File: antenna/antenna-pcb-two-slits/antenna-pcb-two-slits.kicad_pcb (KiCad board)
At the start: 2 copper layers, 97 x 97 mm, 11 parts, among them J1 SMA Connector Male, U1 HHM1589D1

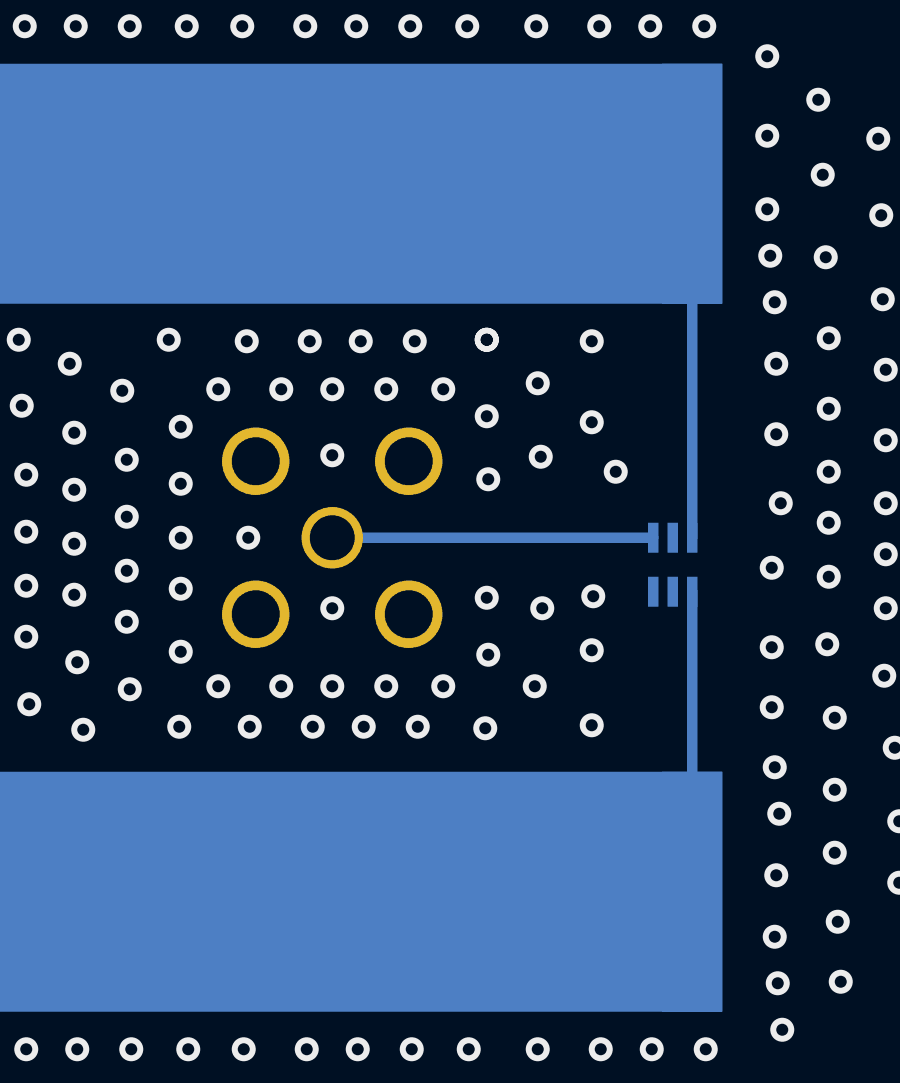
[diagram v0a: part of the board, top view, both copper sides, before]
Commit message: modify antenna pcbs and drc checked
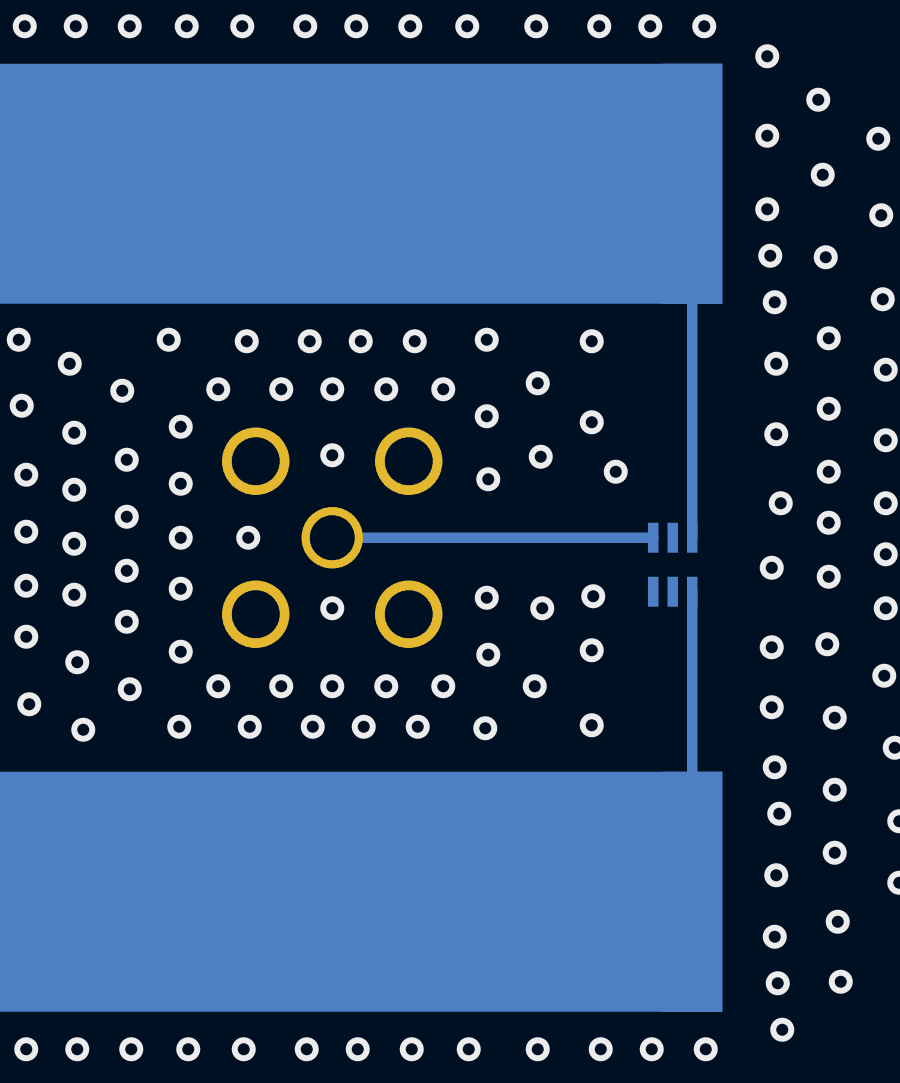
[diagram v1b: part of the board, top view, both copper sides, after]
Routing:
- net Net-(AE1-Pad1): track 23.4 -> 11.8 mm
- net Net-(AE1-Pad2): track 13.9 -> 10.0 mm
- net GND: vias 210 -> 209
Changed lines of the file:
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@@
   )
   (segment (start 130.5 86.7) (end 130.5 98.5) (width 0.35) (layer "B.Cu") (net 2))
-  (segment (start 126.3 89.42) (end 123.58 86.7) (width 0.25) (layer "B.Cu") (net 2))
-  (segment (start 126.3 86.7) (end 118.5 86.7) (width 0.25) (layer "B.Cu") (net 2))
   (via (at 136.95 95.25) (size 0.8) (drill 0.4) (layers "F.Cu" "B.Cu") (free) (net 3))
   (via (at 127.95 96.3) (size 0.8) (drill 0.4) (layers "F.Cu" "B.Cu") (free) (net 3))
@@
   (via (at 108.05 91.9) (size 0.8) (drill 0.4) (layers "F.Cu" "B.Cu") (free) (net 3))
   (via (at 108.3 98.3) (size 0.8) (drill 0.4) (layers "F.Cu" "B.Cu") (free) (net 3))
-  (via (at 123.65 91.9) (size 0.8) (drill 0.4) (layers "F.Cu" "B.Cu") (free) (net 3))
   (via (at 103.85 86.45) (size 0.8) (drill 0.4) (layers "F.Cu" "B.Cu") (free) (net 3))
   (via (at 120.3 93.55) (size 0.8) (drill 0.4) (layers "F.Cu" "B.Cu") (free) (net 3))
@@
   (via (at 135.05 91.85) (size 0.8) (drill 0.4) (layers "F.Cu" "B.Cu") (free) (net 3))
   (via (at 121.25 91.95) (size 0.8) (drill 0.4) (layers "F.Cu" "B.Cu") (free) (net 3))
-  (segment (start 126.35 110.5) (end 126.3 110.55) (width 0.25) (layer "B.Cu") (net 4))
-  (segment (start 126.3 107.58) (end 123.58 110.3) (width 0.25) (layer "B.Cu") (net 4))
   (segment (start 130.5 100.3) (end 130.5 110.3) (width 0.35) (layer "B.Cu") (net 4))
   (segment (start 129.2 98.5) (end 118.5 98.5) (width 0.35) (layer "B.Cu") (net 5))
